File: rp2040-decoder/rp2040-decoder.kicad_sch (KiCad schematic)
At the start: 52 parts, among them J4 5052702412, Q1 TPM2008, Q2 TPM2008, Q3 TPM2008, Q5 TPM2008, Q6 TPM2008, SW1 BOOT, U1 W25Q16JVUXIQ, U2 MT2492, U3 RP2040, U4 MD9927, U5 MAX98357A, Y1 X252012MMB4SI

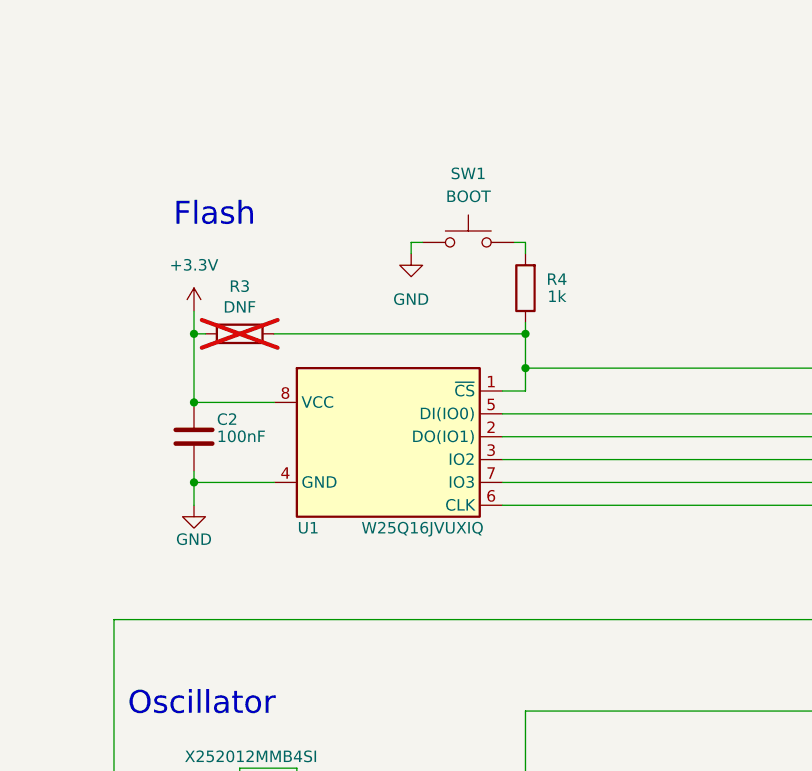
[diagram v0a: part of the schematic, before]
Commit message: feat: upgrade flash to 8MB
feat: reorganize layout to be cleaner
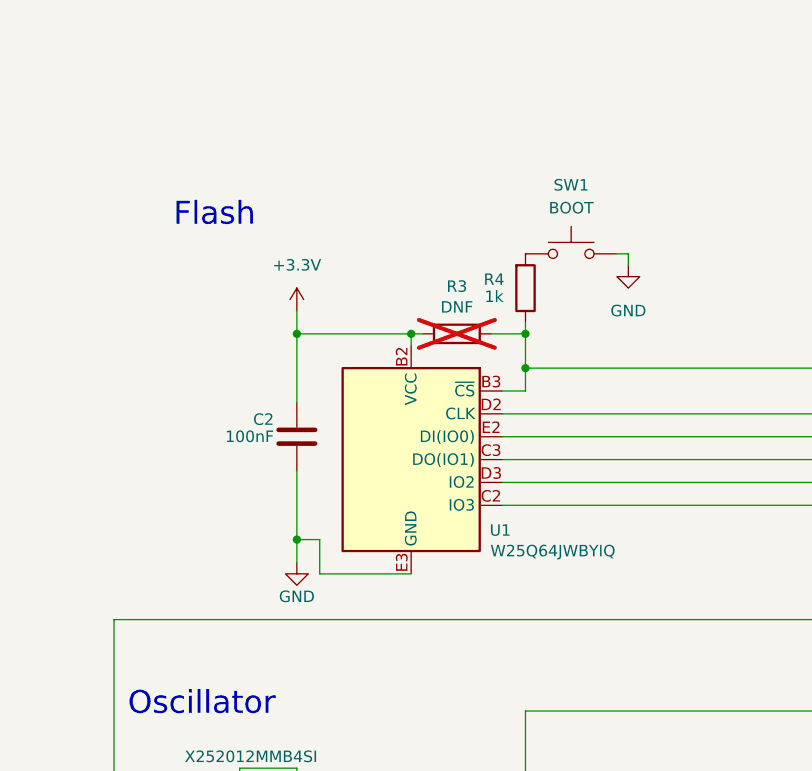
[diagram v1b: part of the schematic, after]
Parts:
- U1: value W25Q16JVUXIQ -> W25Q64JWBYIQ; footprint Package_SON:Winbond_USON-8-1EP_3x2mm_P0.5mm_EP0.2x1.6mm -> Local Library:Winbond_WLCSP-12_P0.5mm; symbol RP2040-Decoder_Additional_Symbols:W25Q64JVSSIQ -> Local Symbol Library:W25Q64JWBYIQ; LCSC C2843335 -> C2691929
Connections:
- net +3.3V: now also U1.B2 (VCC); no longer U1.8 (VCC)
- net GND: now also U1.E3 (GND); no longer U1.4 (GND), U1.9 (GND)
- net at U3.51 (QSPI_SD3): now also U1.D3 (IO2); no longer U1.7 (IO3)
- net at U3.52 (QSPI_SCLK): now also U1.C2 (IO3); no longer U1.6 (CLK)
- net at U3.53 (QSPI_SD0): now also U1.D2 (CLK); no longer U1.5 (DI(IO0))
- net at U3.54 (QSPI_SD2): now also U1.C3 (DO(IO1)); no longer U1.3 (IO2)
- net at U3.55 (QSPI_SD1): now also U1.E2 (DI(IO0)); no longer U1.2 (DO(IO1))
- net at R3.1, R4.1, U3.56 (QSPI_SS): now also U1.B3 (~{CS}); no longer U1.1 (~{CS})
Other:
- moved on the sheet: C2, R3, R4, U1

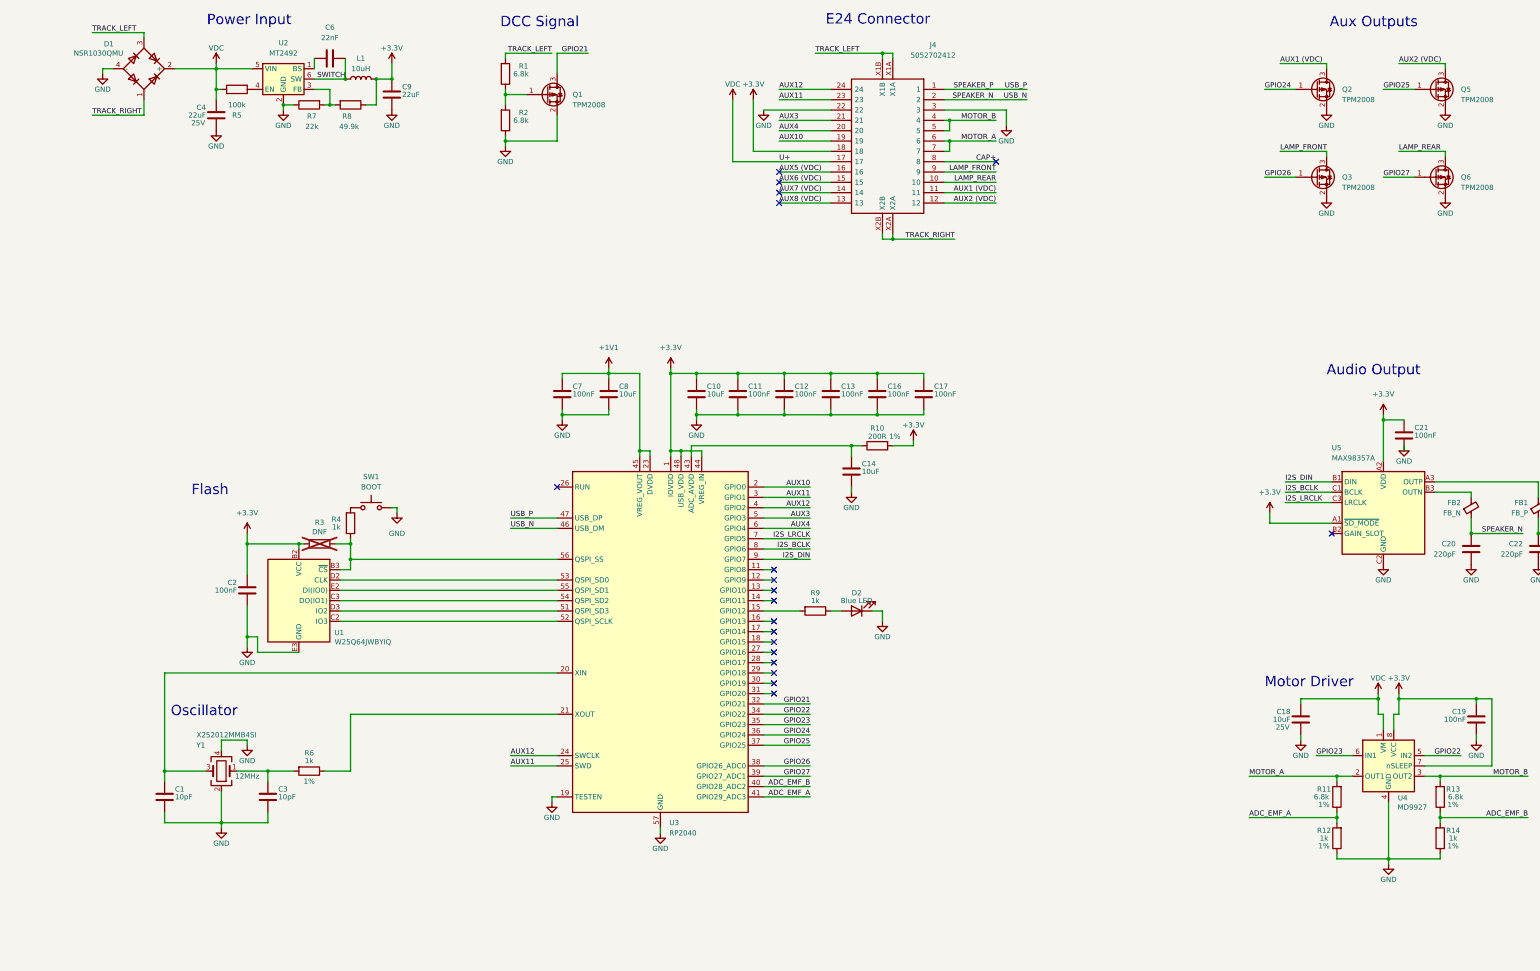
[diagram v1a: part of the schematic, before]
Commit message: feat: add external capacitor support
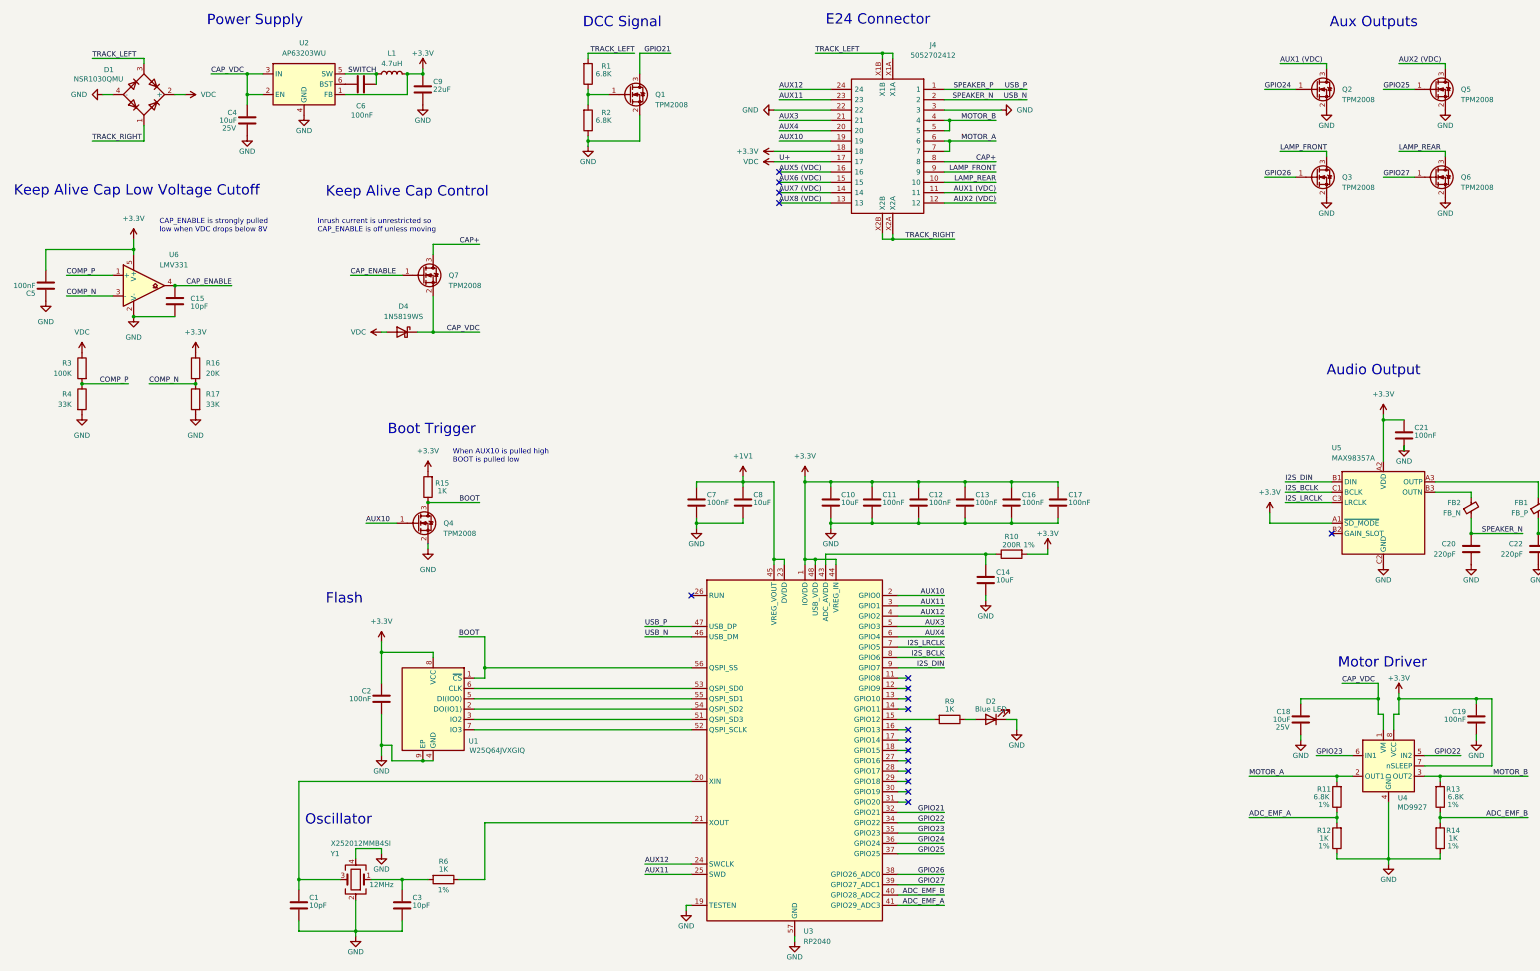
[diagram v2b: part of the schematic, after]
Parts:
- removed R5: 100k, Resistor_SMD:R_0201_0603Metric, symbol Device:R
- removed R7: 22k, Resistor_SMD:R_0201_0603Metric, symbol Device:R
- removed R8: 49.9k, Resistor_SMD:R_0201_0603Metric, symbol Device:R
- removed SW1: BOOT, Local Library:Xunpu_TS-1088-AR02016, symbol Switch:SW_Push
- removed U2: MT2492, Package_TO_SOT_SMD:SOT-23-6, symbol Local Symbol Library:MT2492
- added C15: 10pF, Capacitor_SMD:C_0201_0603Metric, symbol Device:C
- added C5: 100nF, Capacitor_SMD:C_0201_0603Metric, symbol Device:C
- added D4: 1N5819WS, Diode_SMD:D_SOD-323, symbol Device:D_Schottky
- added Q4, Q7: TPM2008, Local Library:Diodes_DFN1006-3, symbol Transistor_FET:2N7002
- added R15: 1K, Resistor_SMD:R_0201_0603Metric, symbol Device:R
- added R16: 20K, Resistor_SMD:R_0201_0603Metric, symbol Device:R
- added R17: 33K, Resistor_SMD:R_0201_0603Metric, symbol Device:R
- added U2: AP63203WU, Package_TO_SOT_SMD:TSOT-23-6, symbol Regulator_Switching:AP63203WU
- added U6: LMV331, Package_TO_SOT_SMD:SOT-353_SC-70-5, symbol Comparator:LMV331
- C4: value 22uF -> 10uF; footprint Capacitor_Tantalum_SMD:CP_EIA-3528-21_Kemet-B -> Capacitor_SMD:C_0603_1608Metric; LCSC C2158664 -> C96446
- C6: value 22nF -> 100nF; LCSC C76934 -> C49062
- C9: LCSC C45783 -> C86295
- L1: value 10uH -> 4.7uH; LCSC C5832376 -> C5832360
- Q1, Q2, Q3, Q5, Q6: symbol Transistor_FET:AO3401A -> Transistor_FET:2N7002
- R1, R11, R13, R2: value 6.8k -> 6.8K
- R12, R14, R6, R9: value 1k -> 1K
- R3: value DNF -> 100K; footprint Resistor_SMD:R_0402_1005Metric -> Resistor_SMD:R_0201_0603Metric; LCSC (none) -> C270364; now fitted; now in the parts list
- R4: value 1k -> 33K; LCSC C270365 -> C473534; Tolerance 10% -> (none)
- U1: value W25Q64JWBYIQ -> W25Q64JVXGIQ; footprint Local Library:Winbond_WLCSP-12_P0.5mm -> Local Library:W25Q64JVXGIQ; symbol Local Symbol Library:W25Q64JWBYIQ -> Memory_Flash:W25Q32JVZP; LCSC C2691929 -> C2940195
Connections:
- net +3.3V: now also U1.8 (VCC), C5.2, R15.2, R16.1, U2.1 (FB), U6.5 (V+); no longer R3.2, U1.B2 (VCC)
- net AUX10: now also Q4.1 (G)
- net CAP+: now also Q7.3 (D)
- net GND: now also R4.2, U1.4 (GND), U1.9 (EP), C15.2, C5.1, Q4.2 (S), R17.2, U2.4 (GND), U6.2 (V-); no longer U1.E3 (GND)
- net SWITCH: now also U2.5 (SW)
- net VDC: now also R3.1, D4.2 (A); no longer C18.1, C4.1, U4.1 (VM)
- net at C6.1: now also U2.6 (BST)
- net at U3.51 (QSPI_SD3): now also U1.3 (IO2); no longer U1.D3 (IO2)
- net at U3.52 (QSPI_SCLK): now also U1.7 (IO3); no longer U1.C2 (IO3)
- net at U3.53 (QSPI_SD0): now also U1.6 (CLK); no longer U1.D2 (CLK)
- net at U3.54 (QSPI_SD2): now also U1.2 (DO(IO1)); no longer U1.C3 (DO(IO1))
- net at U3.55 (QSPI_SD1): now also U1.5 (DI(IO0)); no longer U1.E2 (DI(IO0))
- new net BOOT: Q4.3 (D), R15.1, U1.1 (~{CS}), U3.56 (QSPI_SS)
- new net CAP_ENABLE: C15.1, Q7.1 (G), U6.4
- new net CAP_VDC: C18.1, C4.1, D4.1 (K), Q7.2 (S), U2.2 (EN), U2.3 (IN), U4.1 (VM)
- new net COMP_N: R16.2, R17.1, U6.3 (-)
- new net COMP_P: R3.2, R4.1, U6.1 (+)
- no-connect marks 19 -> 18
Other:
- note added: "Boot Trigger"
- note added: "CAP_ENABLE is strongly pulled low when VDC drops below 8V"
- note added: "Inrush current is unrestricted so CAP_ENABLE is off unless moving"
- note added: "Keep Alive Cap Control"
- note added: "Keep Alive Cap Low Voltage Cutoff"
- note added: "Power Supply"
- note added: "When AUX10 is pulled high BOOT is pulled low"
- note removed: "Power Input"
- moved on the sheet: C1, C10, C11, C12, C13, C14, C16, C17, C2, C3, C4, C6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

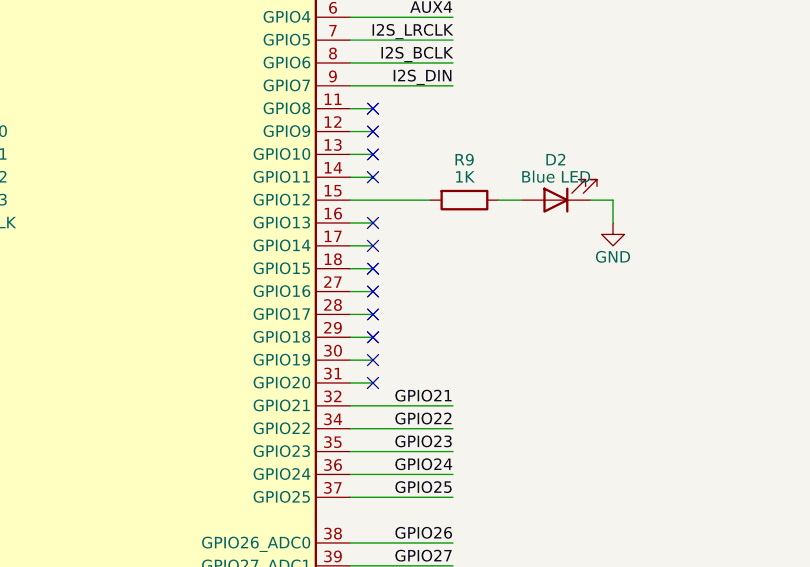
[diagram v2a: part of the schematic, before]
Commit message: fix: dfm fixes and trace cleanup
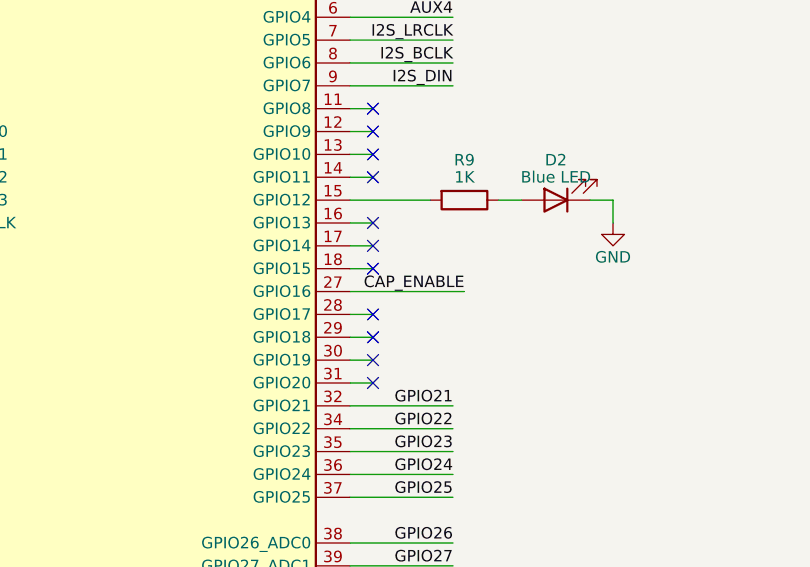
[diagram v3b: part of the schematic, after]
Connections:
- net CAP_ENABLE: now also U3.27 (GPIO16)
- no-connect marks 18 -> 17
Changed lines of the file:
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@@
 	)
 	(no_connect
-		(at 237.49 212.09)
-	)
-	(no_connect
 		(at 205.74 74.93)
 	)
@@
 	(wire
 		(pts
-			(xy 234.95 212.09) (xy 237.49 212.09)
-		)
-		(stroke
-			(width 0)
-			(type default)
-		)
-	)
-	(wire
-		(pts
 			(xy 274.32 143.51) (xy 274.32 144.78)
 		)
@@
 	(wire
 		(pts
+			(xy 234.95 212.09) (xy 247.65 212.09)
+		)
+		(stroke
+			(width 0)
+			(type default)
+		)
+	)
+	(wire
+		(pts
 			(xy 234.95 217.17) (xy 237.49 217.17)
 		)
@@
 		(effects
 			(font
+				(size 1.27 1.27)
+			)
+			(justify right bottom)
+		)
+	)
+	(label "CAP_ENABLE"
+		(at 247.65 212.09 180)
+		(effects
+			(font
